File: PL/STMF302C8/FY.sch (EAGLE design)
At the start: 51 parts, among them J1 CON-SD-CARD_MICROSD-2908-05, J2 Flash Programming, U1 AS72652-BLGT, U2 AS72653-BLGT, U3 STM32F302C8T6, U4 AS72651-BLGT, U5 AMS1117-3.3, U6 4MB Flash, Y2 ABM2B-8.000MHZ-10-1-U-T

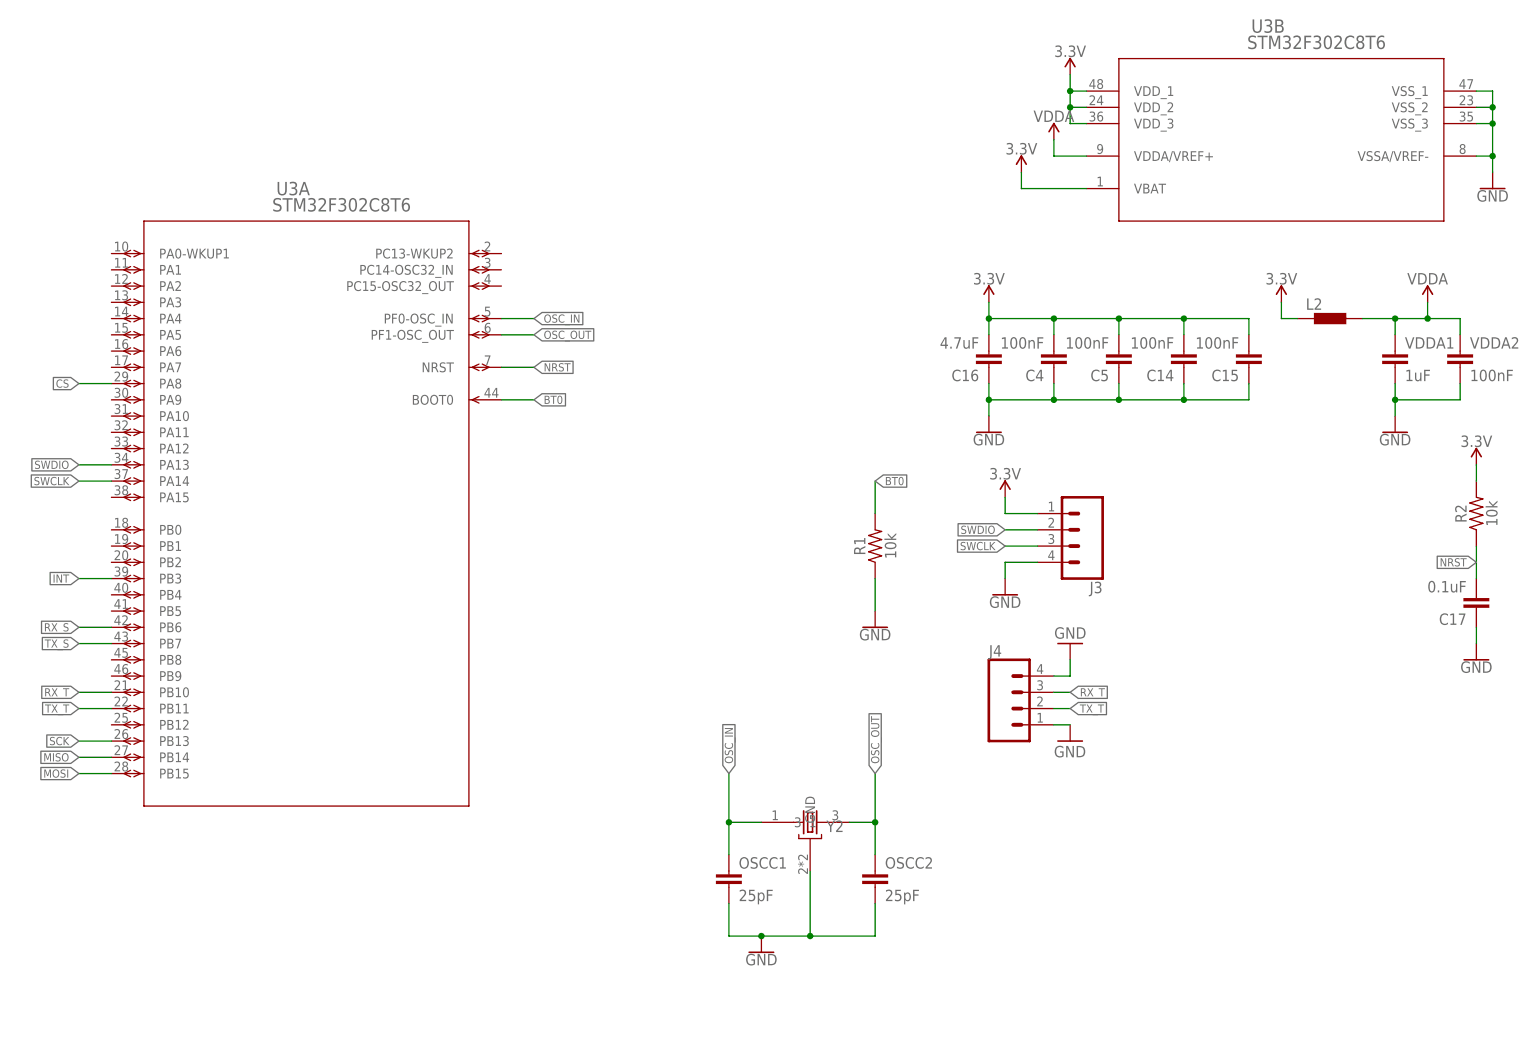
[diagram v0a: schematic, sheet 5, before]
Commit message: Connector was changed and Preparing first order
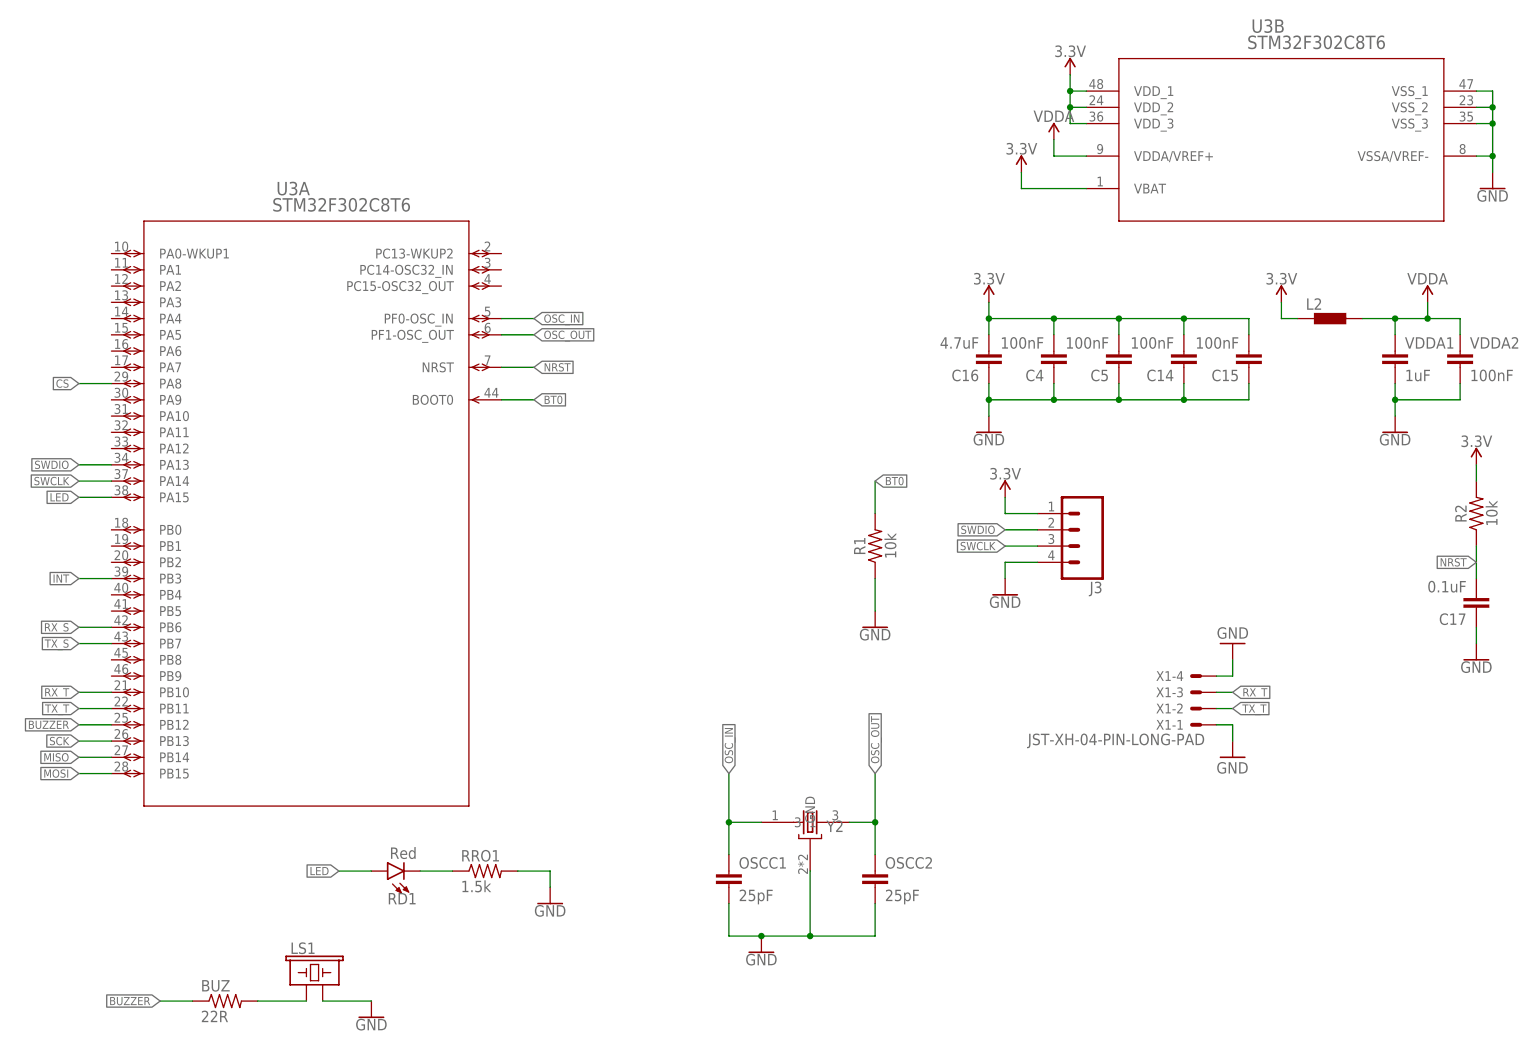
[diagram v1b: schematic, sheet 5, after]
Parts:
- removed J4: (no value), SparkFun-Connectors:CONN_04JST-PTH-VERT
- added BUZ: 22R, SparkFun-Resistors:2.0KOHM1/10W5%(0603)
- added LS1: BUZZER-PTH, SparkFun-Electromechanical:BUZZER-PTH
- added RD1: Red, SparkFun-LED:LED-RED0603-SMART
- added RRO1: 1.5k, SparkFun-Resistors:2.0KOHM1/10W5%(0603)
- added X1: JST-XH-04-PIN-LONG-PAD, Rembrandt Electronics - JST XH Connectors v1-0:JST-XH-04-PIN-LONG-PAD
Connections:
- new net BUZZER: BUZ.1, U3A.PB12
- new net LED: RD1.A, U3A.PA15
- new net N$13: BUZ.2, LS1.1
- new net N$2: RD1.C, RRO1.1
- net GND: now also LS1.2, RRO1.2, X1-1.S, X1-4.S; no longer J4.1, J4.4
- net RX_T: now also X1-3.S; no longer J4.3
- net TX_T: now also X1-2.S; no longer J4.2

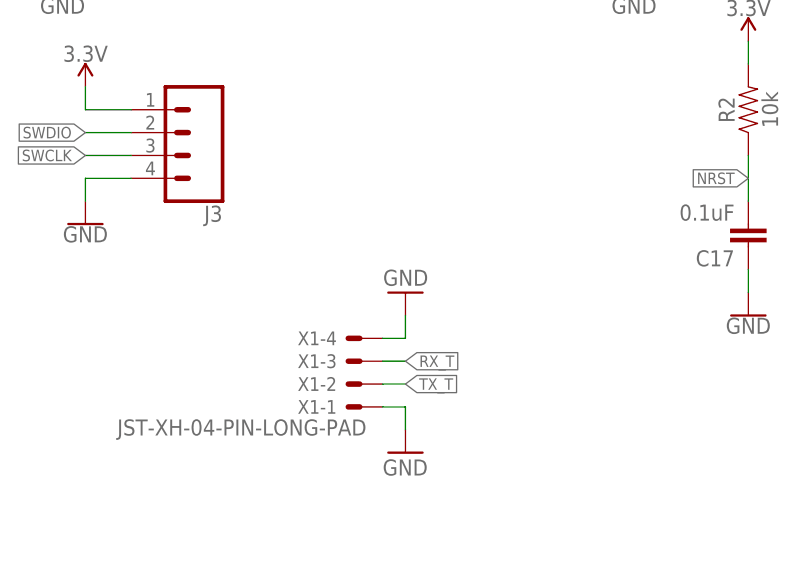
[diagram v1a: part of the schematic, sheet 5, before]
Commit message: Polygon witdh was increased IMPOTANT**
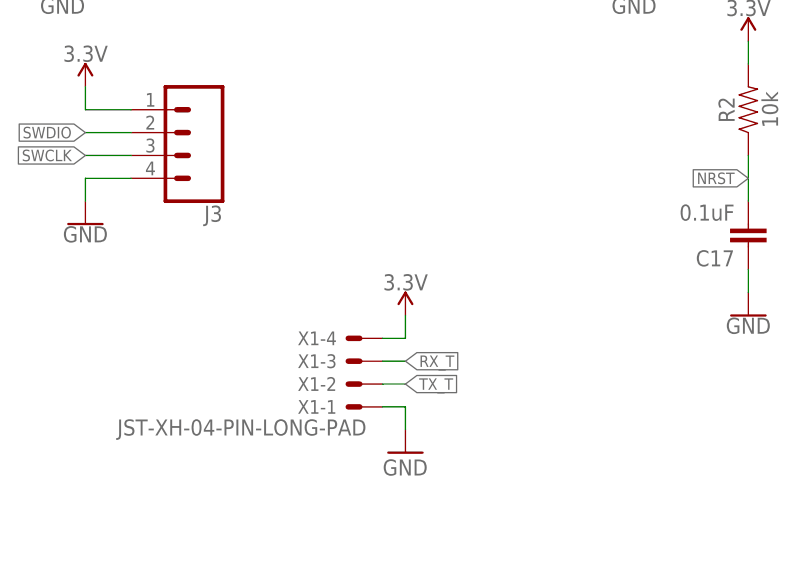
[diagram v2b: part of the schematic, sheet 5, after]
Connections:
- net 3.3V: now also X1-4.S
- net GND: no longer X1-4.S
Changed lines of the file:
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@@
 <part name="GND8" library="SparkFun-PowerSymbols" library_urn="urn:adsk.eagle:library:530" deviceset="GND" device=""/>
 <part name="X1" library="Rembrandt Electronics - JST XH Connectors v1-0" deviceset="JST-XH-04-PIN" device="-LONG-PAD"/>
-<part name="GND24" library="supply1" library_urn="urn:adsk.eagle:library:371" deviceset="GND" device=""/>
 <part name="GND27" library="supply1" library_urn="urn:adsk.eagle:library:371" deviceset="GND" device=""/>
+<part name="SUPPLY13" library="SparkFun-PowerSymbols" deviceset="3.3V" device=""/>
 </parts>
 <sheets>
@@
 <attribute name="NAME" x="218.44" y="76.962" size="1.524" layer="95" rot="R180"/>
 </instance>
-<instance part="GND24" gate="1" x="226.06" y="81.28" smashed="yes" rot="R180">
-<attribute name="VALUE" x="228.6" y="83.82" size="1.778" layer="96" rot="R180"/>
-</instance>
 <instance part="GND27" gate="1" x="226.06" y="63.5" smashed="yes">
 <attribute name="VALUE" x="223.52" y="60.96" size="1.778" layer="96"/>
+</instance>
+<instance part="SUPPLY13" gate="G$1" x="226.06" y="78.74" smashed="yes">
+<attribute name="VALUE" x="226.06" y="81.534" size="1.778" layer="96" align="bottom-center"/>
 </instance>
 </instances>
@@
 </segment>
 <segment>
-<pinref part="X1" gate="-4" pin="S"/>
-<wire x1="223.52" y1="76.2" x2="226.06" y2="76.2" width="0.1524" layer="91"/>
-<pinref part="GND24" gate="1" pin="GND"/>
-<wire x1="226.06" y1="76.2" x2="226.06" y2="78.74" width="0.1524" layer="91"/>
-</segment>
-<segment>
 <pinref part="X1" gate="-1" pin="S"/>
 <wire x1="223.52" y1="68.58" x2="226.06" y2="68.58" width="0.1524" layer="91"/>
@@
 <wire x1="193.04" y1="152.4" x2="203.2" y2="152.4" width="0.1524" layer="91"/>
 </segment>
-</net>
+<segment>
+<pinref part="X1" gate="-4" pin="S"/>
+<wire x1="223.52" y1="76.2" x2="226.06" y2="76.2" width="0.1524" layer="91"/>
+<pinref part="SUPPLY13" gate="G$1" pin="3.3V"/>
+<wire x1="226.06" y1="76.2" x2="226.06" y2="78.74" width="0.1524" layer="91"/>
+</segment>
+</net>

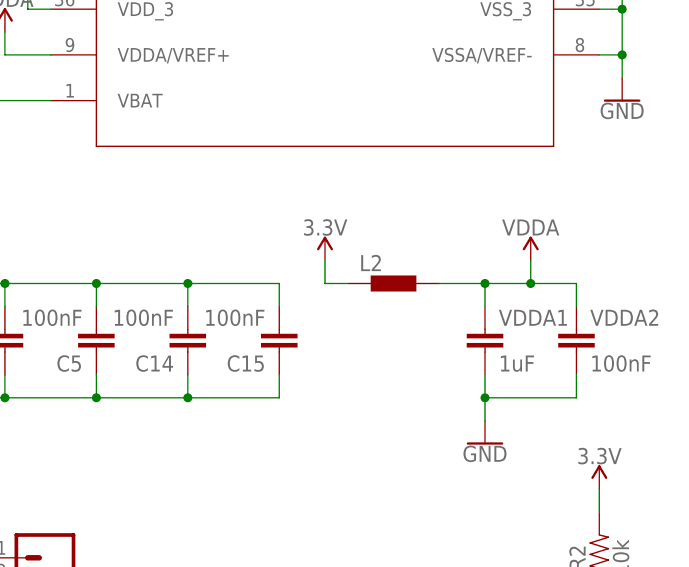
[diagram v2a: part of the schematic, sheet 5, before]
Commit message: packages was modified according to stock situation
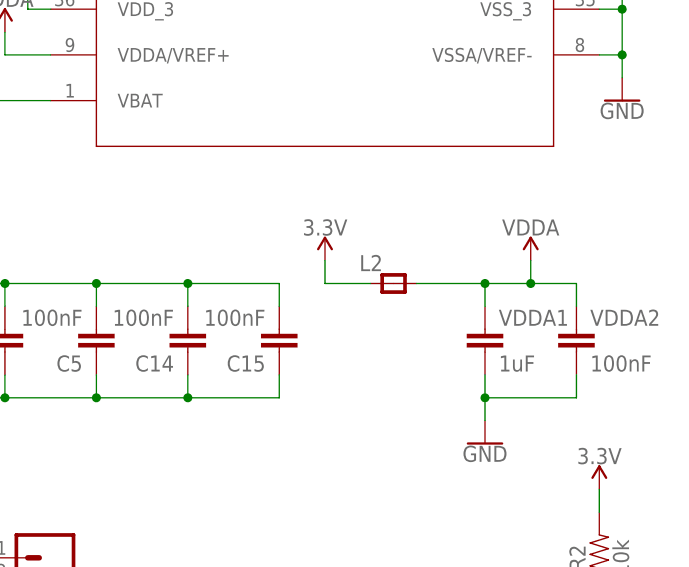
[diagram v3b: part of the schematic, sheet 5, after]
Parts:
- L2: value BLM15HB221SN1 -> (none); device inductors:BLM15HB221SN1 -> 52101-101-REV-A_v16:RC-MASTER-SMD_FB_0805MP
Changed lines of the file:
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@@
 <part name="VDDA2" library="SparkFun-Capacitors" library_urn="urn:adsk.eagle:library:510" deviceset="0.1UF" device="-0603-25V-(+80/-20%)" package3d_urn="urn:adsk.eagle:package:37414/1" value="100nF"/>
 <part name="GND9" library="SparkFun-PowerSymbols" library_urn="urn:adsk.eagle:library:530" deviceset="GND" device=""/>
-<part name="L2" library="inductors" library_urn="urn:adsk.eagle:library:243" deviceset="BLM15H" device="" package3d_urn="urn:adsk.eagle:package:15132/1" technology="B221SN1">
+<part name="L2" library="52101-101-REV-A_v16" library_urn="urn:adsk.eagle:library:21899384" deviceset="RC-MASTER-SMD_FB_" device="0805MP" package3d_urn="urn:adsk.eagle:package:15662270/2">
 <attribute name="ORDER_URL" value="https://eu.mouser.com/ProductDetail/Murata-Electronics/NFZ15SR152SN10D?qs=rkhjVJ6%2F3EK7NITaH%252B9%252Bxg%3D%3D"/>
 </part>
@@
 <wire x1="233.68" y1="134.62" x2="233.68" y2="132.08" width="0.1524" layer="91"/>
 <pinref part="L2" gate="G$1" pin="1"/>
-<wire x1="233.68" y1="132.08" x2="236.22" y2="132.08" width="0.1524" layer="91"/>
+<wire x1="233.68" y1="132.08" x2="238.76" y2="132.08" width="0.1524" layer="91"/>
 </segment>
 <segment>
@@
 <pinref part="L2" gate="G$1" pin="2"/>
 <pinref part="VDDA2" gate="G$1" pin="1"/>
-<wire x1="246.38" y1="132.08" x2="251.46" y2="132.08" width="0.1524" layer="91"/>
+<wire x1="243.84" y1="132.08" x2="251.46" y2="132.08" width="0.1524" layer="91"/>
 <wire x1="251.46" y1="132.08" x2="256.54" y2="132.08" width="0.1524" layer="91"/>
 <wire x1="256.54" y1="132.08" x2="261.62" y2="132.08" width="0.1524" layer="91"/>
